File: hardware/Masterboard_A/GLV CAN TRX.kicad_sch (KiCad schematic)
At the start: 11 parts, among them U10 MCP2542FDxMF, U3 L78L05_SOT89, U5 ISO7721D

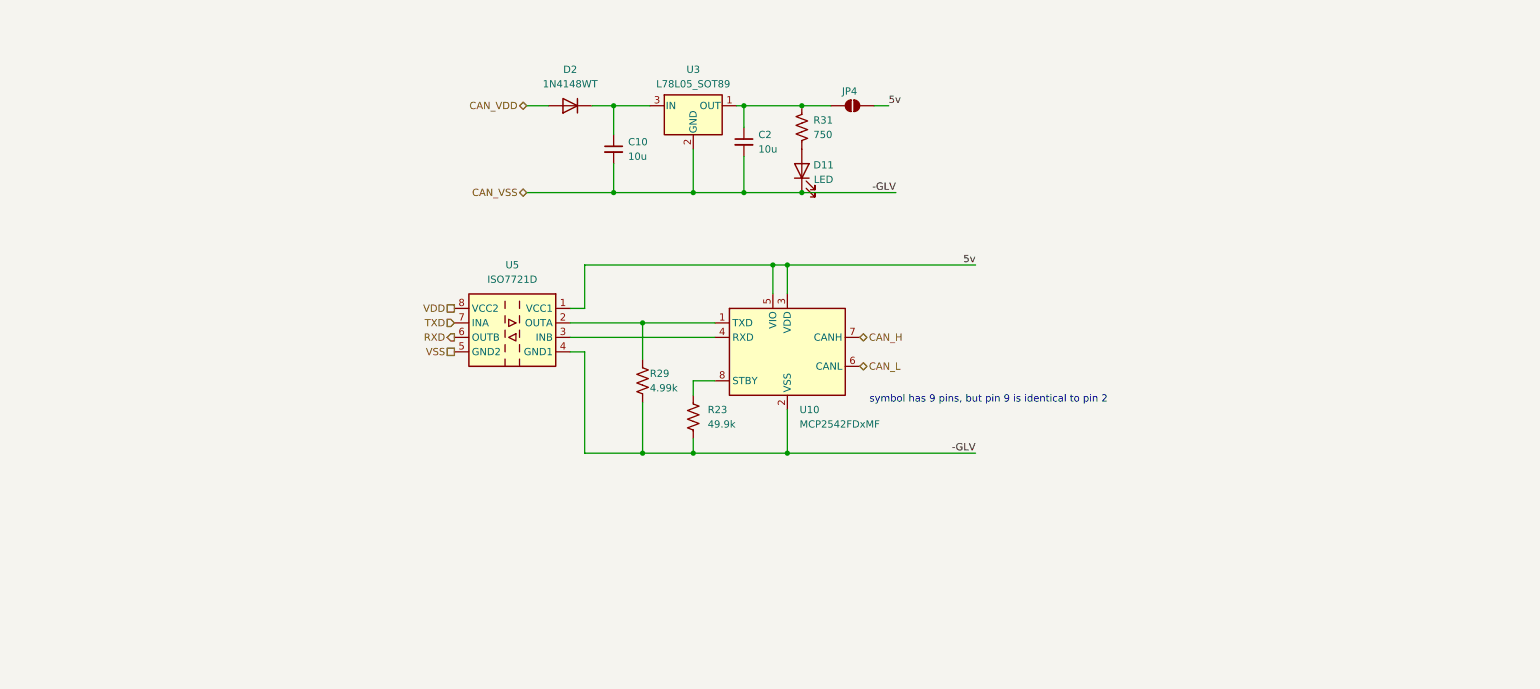
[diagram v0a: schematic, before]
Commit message: basic psu for master board
we scrapping the onboard HRLV supply. solution is "thats not our problem", if they dont want HV on the LV then they should isolate it, not us.
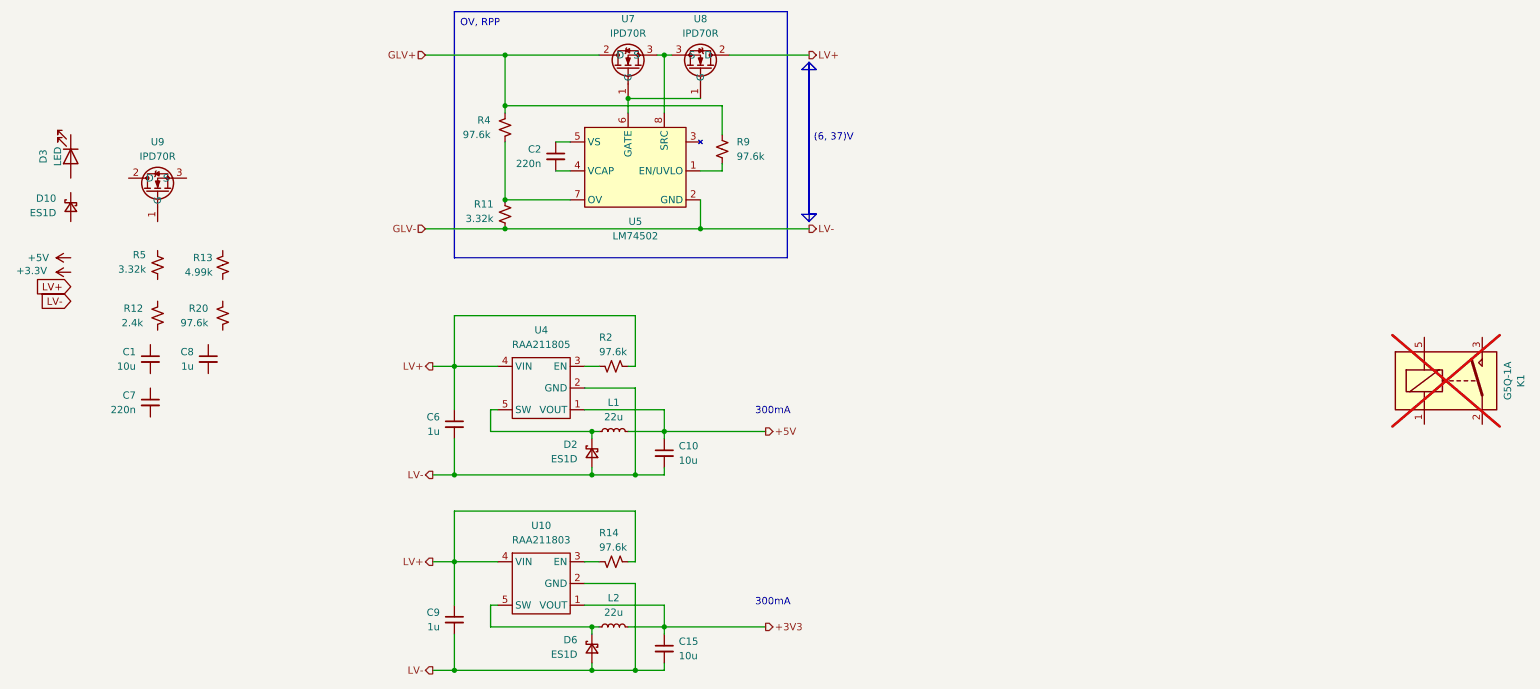
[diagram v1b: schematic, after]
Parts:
- removed D11: LED, LED_SMD:LED_0603_1608Metric, symbol Device:LED
- removed D2: 1N4148WT, Diode_SMD:D_SOD-523, symbol Diode:1N4148WT
- removed JP4: SolderJumper_2_Open, Jumper:SolderJumper-2_P1.3mm_Open_TrianglePad1.0x1.5mm, symbol Jumper:SolderJumper_2_Open
- removed R23: 49.9k, Resistor_SMD:R_1206_3216Metric_Pad1.30x1.75mm_HandSolder, symbol Device:R_US
- removed R29: 4.99k, Resistor_SMD:R_1206_3216Metric_Pad1.30x1.75mm_HandSolder, symbol Device:R_US
- removed R31: 750, Resistor_SMD:R_1206_3216Metric_Pad1.30x1.75mm_HandSolder, symbol Device:R_US
- removed U10: MCP2542FDxMF, zzLocalLibraries-Footprints:SOIC-8_4.9x6.0mm_P1.27mm, symbol Interface_CAN_LIN:MCP2542FDxMF
- removed U3: L78L05_SOT89, Package_TO_SOT_SMD:SOT-89-3, symbol Regulator_Linear:L78L05_SOT89
- removed U5: ISO7721D, Package_SO:SOIC-8_3.9x4.9mm_P1.27mm, symbol Isolator:ISO7721D
- added C1, C15: 10u, Capacitor_SMD:C_1206_3216Metric_Pad1.33x1.80mm_HandSolder, symbol Device:C_Small
- added C6, C8, C9: 1u, Capacitor_SMD:C_1206_3216Metric_Pad1.33x1.80mm_HandSolder, symbol Device:C_Small
- added C7: 220n, Capacitor_SMD:C_1206_3216Metric_Pad1.33x1.80mm_HandSolder, symbol Device:C_Small
- added D10, D2, D6: ES1D, Diode_SMD:D_SMA, symbol Device:D_Schottky_Small
- added D3: LED, LED_SMD:LED_0603_1608Metric, symbol Device:LED
- added K1: G5Q-1A, Relay_THT:Relay_SPST_Omron-G5Q-1A, symbol Relay:G5Q-1A
- added L1, L2: 22u, Inductor_SMD:L_1210_3225Metric_Pad1.42x2.65mm_HandSolder, symbol Device:L_Small
- added R11, R5: 3.32k, Resistor_SMD:R_0805_2012Metric_Pad1.20x1.40mm_HandSolder, symbol Device:R_Small_US
- added R12: 2.4k, Resistor_SMD:R_0805_2012Metric_Pad1.20x1.40mm_HandSolder, symbol Device:R_Small_US
- added R13: 4.99k, Resistor_SMD:R_1206_3216Metric_Pad1.30x1.75mm_HandSolder, symbol Device:R_Small_US
- added R14, R2, R20, R4, R9: 97.6k, Resistor_SMD:R_0805_2012Metric_Pad1.20x1.40mm_HandSolder, symbol Device:R_Small_US
- added U10: RAA211803, Package_TO_SOT_SMD:TSOT-23-5, symbol zzLocalLibrary:RAA211803
- added U4: RAA211805, Package_TO_SOT_SMD:TSOT-23-5, symbol zzLocalLibrary:RAA211805
- added U5: LM74502, Package_TO_SOT_SMD:SOT-23-8_Handsoldering, symbol zzLocalLibrary:LM74502
- added U7, U8, U9: IPD70R, Package_TO_SOT_SMD:TO-252-2, symbol zzLocalLibrary:IPD70R
- C2: value 10u -> 220n; mouser https://www.mouser.com/ProductDetail/Samsung-Electro-Mechanics/CL31A106KBHNNNE?qs=sGAEpiMZZMsh%252B1woXyUXjxqcB7t9naYpzWmpMbMJIKQ%3D -> https://www.mouser.com/ProductDetail/Samsung-Electro-Mechanics/CL31B224KBFNNNF?qs=sGAEpiMZZMsh%252B1woXyUXj7iNKXiFkBmw7C%252BUlKpuDJ8%3D; specs 10uF, 50VDC, X5R, 10%, -55C, +85C -> 50VDC, X7R, 10%, -55C, +125C, 220nF; unit x10 0.07 -> 0.054
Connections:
- net +5V: now reaches C10.1
- net +5V: now also L1.2, U4.1 (VOUT)
- net at C2.1: now also U5.5 (VS)
- net CAN_VSS: no longer names the net of C2.2
- net CAN_VSS: now also U5.4 (VCAP); no longer C10.2
- new net: R11.2, R4.1, U5.7 (OV)
- new net: D6.1 (K), L2.1, U10.5 (SW)
- new net: D2.1 (K), L1.1, U4.5 (SW)
- new net: R2.1, U4.3 (EN)
- new net: U5.6 (GATE), U7.1 (G), U8.1 (G)
- new net: U5.8 (SRC), U7.3 (S), U8.3 (S)
- new net: R9.1, U5.1 (EN/UVLO)
- new net: R14.1, U10.3 (EN)
- new net +3V3: C15.1, L2.2, U10.1 (VOUT)
- new net GLV+: R4.2, R9.2, U7.2 (D)
- new net LV+: C6.1, C9.1, R14.2, R2.2, U10.4 (VIN), U4.4 (VIN), U8.2 (D)
- new net LV-: C10.2, C15.2, C6.2, C9.2, D2.2 (A), D6.2 (A), R11.1, U10.2 (GND), U4.2 (GND), U5.2 (GND)
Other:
- note added: "(6, 37)V"
- note added: "300mA"
- note added: "OV, RPP"
- note removed: "symbol has 9 pins, but pin 9 is identical to pin 2"
- moved on the sheet: C10

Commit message: ungodly amount of master board hardware todos
todo to do to do do do dooo
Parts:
- removed C1: 10u, Capacitor_SMD:C_1206_3216Metric_Pad1.33x1.80mm_HandSolder, symbol Device:C_Small
- removed C7: 220n, Capacitor_SMD:C_1206_3216Metric_Pad1.33x1.80mm_HandSolder, symbol Device:C_Small
- removed C8: 1u, Capacitor_SMD:C_1206_3216Metric_Pad1.33x1.80mm_HandSolder, symbol Device:C_Small
- removed D10: ES1D, Diode_SMD:D_SMA, symbol Device:D_Schottky_Small
- removed D3: LED, LED_SMD:LED_0603_1608Metric, symbol Device:LED
- removed K1: G5Q-1A, Relay_THT:Relay_SPST_Omron-G5Q-1A, symbol Relay:G5Q-1A
- removed R12: 2.4k, Resistor_SMD:R_0805_2012Metric_Pad1.20x1.40mm_HandSolder, symbol Device:R_Small_US
- removed R13: 4.99k, Resistor_SMD:R_1206_3216Metric_Pad1.30x1.75mm_HandSolder, symbol Device:R_Small_US
- removed R20: 97.6k, Resistor_SMD:R_0805_2012Metric_Pad1.20x1.40mm_HandSolder, symbol Device:R_Small_US
- removed R5: 3.32k, Resistor_SMD:R_0805_2012Metric_Pad1.20x1.40mm_HandSolder, symbol Device:R_Small_US
- removed U9: IPD70R, Package_TO_SOT_SMD:TO-252-2, symbol zzLocalLibrary:IPD70R
- added TP5, TP6: TestPoint, TestPoint:TestPoint_Loop_D2.50mm_Drill1.0mm_LowProfile, symbol Connector:TestPoint
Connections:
- net +3V3: now also TP6.1
- net +5V: now also TP5.1
- net GLV+: now also C2.1, U5.5 (VS)
- net LV- renamed GLV-
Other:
- moved on the sheet: R4, R9
